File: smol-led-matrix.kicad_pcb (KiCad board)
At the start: 4 copper layers, 61.8 x 88.2 mm, 381 parts, among them J1 USB_C_Receptacle_USB2.0, J2 TagConnect_TC2030_SWD, Q1 FS8205, Q2 AO3401A, SW1 SW_Push, SW2 SW_Push, U1 STM32L433CBTx, U2 TP4054, U3 DW01+G, U4 XC6206P332MR

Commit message: Full panel
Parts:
- added C1: 100nF, Capacitor_SMD:C_0402_1005Metric, F.Cu at (94.8, 86.5)
- added C1: 100nF, Capacitor_SMD:C_0402_1005Metric, F.Cu at (94.8, 115.5)
- added C10: 10uF, Capacitor_SMD:C_0402_1005Metric, F.Cu at (99.9, 82.8)
- added C10: 10uF, Capacitor_SMD:C_0402_1005Metric, F.Cu at (99.9, 111.8)
- added C11: 100nF, Capacitor_SMD:C_0402_1005Metric, F.Cu at (88.2, 76.7)
- added C11: 100nF, Capacitor_SMD:C_0402_1005Metric, F.Cu at (88.2, 105.7)
- added C2: 100nF, Capacitor_SMD:C_0402_1005Metric, F.Cu at (88.0, 83.4)
- added C2: 100nF, Capacitor_SMD:C_0402_1005Metric, F.Cu at (88.0, 112.4)
- added C3: 1uF, Capacitor_SMD:C_0402_1005Metric, F.Cu at (100.5, 70.7)
- added C3: 1uF, Capacitor_SMD:C_0402_1005Metric, F.Cu at (100.5, 99.7)
- added C4: 100nF, Capacitor_SMD:C_0402_1005Metric, F.Cu at (107.0, 70.3)
- added C4: 100nF, Capacitor_SMD:C_0402_1005Metric, F.Cu at (107.0, 99.3)
- added C5: 100nF, Capacitor_SMD:C_0402_1005Metric, F.Cu at (93.0, 86.5)
- added C5: 100nF, Capacitor_SMD:C_0402_1005Metric, F.Cu at (93.0, 115.5)
- added C6: 1uF, Capacitor_SMD:C_0402_1005Metric, F.Cu at (101.9, 78.9)
- added C6: 1uF, Capacitor_SMD:C_0402_1005Metric, F.Cu at (101.9, 107.9)
- added C7: 1uF, Capacitor_SMD:C_0402_1005Metric, F.Cu at (103.6, 78.9)
- added C7: 1uF, Capacitor_SMD:C_0402_1005Metric, F.Cu at (103.6, 107.9)
- added C8: 100nF, Capacitor_SMD:C_0402_1005Metric, F.Cu at (89.2, 77.0)
- added C8: 100nF, Capacitor_SMD:C_0402_1005Metric, F.Cu at (89.2, 106.0)
- added C9: 100nF, Capacitor_SMD:C_0402_1005Metric, F.Cu at (97.5, 77.0)
- added C9: 100nF, Capacitor_SMD:C_0402_1005Metric, F.Cu at (97.5, 106.0)
- added D1: LED, LED_SMD:LED_0402_1005Metric, F.Cu at (63.2, 67.7)
- added D1: LED, LED_SMD:LED_0402_1005Metric, F.Cu at (63.2, 96.7)
- added D10: LED, LED_SMD:LED_0402_1005Metric, F.Cu at (63.2, 79.4)
- added D10: LED, LED_SMD:LED_0402_1005Metric, F.Cu at (63.2, 108.4)
- added D100: LED, LED_SMD:LED_0402_1005Metric, F.Cu at (71.0, 79.4)
- added D100: LED, LED_SMD:LED_0402_1005Metric, F.Cu at (71.0, 108.4)
- added D101: LED, LED_SMD:LED_0402_1005Metric, F.Cu at (71.0, 80.7)
- added D101: LED, LED_SMD:LED_0402_1005Metric, F.Cu at (71.0, 109.7)
- added D102: LED, LED_SMD:LED_0402_1005Metric, F.Cu at (71.0, 82.0)
- added D102: LED, LED_SMD:LED_0402_1005Metric, F.Cu at (71.0, 111.0)
- added D103: LED, LED_SMD:LED_0402_1005Metric, F.Cu at (71.0, 83.3)
- added D103: LED, LED_SMD:LED_0402_1005Metric, F.Cu at (71.0, 112.3)
- added D104: LED, LED_SMD:LED_0402_1005Metric, F.Cu at (71.0, 84.6)
- added D104: LED, LED_SMD:LED_0402_1005Metric, F.Cu at (71.0, 113.6)
- added D105: LED, LED_SMD:LED_0402_1005Metric, F.Cu at (71.0, 85.9)
- added D105: LED, LED_SMD:LED_0402_1005Metric, F.Cu at (71.0, 114.9)
- added D106: LED, LED_SMD:LED_0402_1005Metric, F.Cu at (72.3, 67.7)
- added D106: LED, LED_SMD:LED_0402_1005Metric, F.Cu at (72.3, 96.7)
- added D107: LED, LED_SMD:LED_0402_1005Metric, F.Cu at (72.3, 69.0)
- added D107: LED, LED_SMD:LED_0402_1005Metric, F.Cu at (72.3, 98.0)
- added D108: LED, LED_SMD:LED_0402_1005Metric, F.Cu at (72.3, 70.3)
- added D108: LED, LED_SMD:LED_0402_1005Metric, F.Cu at (72.3, 99.3)
- added D109: LED, LED_SMD:LED_0402_1005Metric, F.Cu at (72.3, 71.6)
- added D109: LED, LED_SMD:LED_0402_1005Metric, F.Cu at (72.3, 100.6)
- added D11: LED, LED_SMD:LED_0402_1005Metric, F.Cu at (63.2, 80.7)
- added D11: LED, LED_SMD:LED_0402_1005Metric, F.Cu at (63.2, 109.7)
- added D110: LED, LED_SMD:LED_0402_1005Metric, F.Cu at (72.3, 72.9)
- added D110: LED, LED_SMD:LED_0402_1005Metric, F.Cu at (72.3, 101.9)
- added D111: LED, LED_SMD:LED_0402_1005Metric, F.Cu at (72.3, 74.2)
- added D111: LED, LED_SMD:LED_0402_1005Metric, F.Cu at (72.3, 103.2)
- added D112: LED, LED_SMD:LED_0402_1005Metric, F.Cu at (72.3, 75.5)
- added D112: LED, LED_SMD:LED_0402_1005Metric, F.Cu at (72.3, 104.5)
- added D113: LED, LED_SMD:LED_0402_1005Metric, F.Cu at (72.3, 76.8)
- added D113: LED, LED_SMD:LED_0402_1005Metric, F.Cu at (72.3, 105.8)
- added D114: LED, LED_SMD:LED_0402_1005Metric, F.Cu at (72.3, 78.1)
- added D114: LED, LED_SMD:LED_0402_1005Metric, F.Cu at (72.3, 107.1)
- added D115: LED, LED_SMD:LED_0402_1005Metric, F.Cu at (72.3, 79.4)
- added D115: LED, LED_SMD:LED_0402_1005Metric, F.Cu at (72.3, 108.4)
- added D116: LED, LED_SMD:LED_0402_1005Metric, F.Cu at (72.3, 80.7)
- added D116: LED, LED_SMD:LED_0402_1005Metric, F.Cu at (72.3, 109.7)
- added D117: LED, LED_SMD:LED_0402_1005Metric, F.Cu at (72.3, 82.0)
- added D117: LED, LED_SMD:LED_0402_1005Metric, F.Cu at (72.3, 111.0)
- added D118: LED, LED_SMD:LED_0402_1005Metric, F.Cu at (72.3, 83.3)
- added D118: LED, LED_SMD:LED_0402_1005Metric, F.Cu at (72.3, 112.3)
- added D119: LED, LED_SMD:LED_0402_1005Metric, F.Cu at (72.3, 84.6)
- added D119: LED, LED_SMD:LED_0402_1005Metric, F.Cu at (72.3, 113.6)
- added D12: LED, LED_SMD:LED_0402_1005Metric, F.Cu at (63.2, 82.0)
- added D12: LED, LED_SMD:LED_0402_1005Metric, F.Cu at (63.2, 111.0)
- added D120: LED, LED_SMD:LED_0402_1005Metric, F.Cu at (72.3, 85.9)
- added D120: LED, LED_SMD:LED_0402_1005Metric, F.Cu at (72.3, 114.9)
- added D121: LED, LED_SMD:LED_0402_1005Metric, F.Cu at (73.6, 67.7)
- added D121: LED, LED_SMD:LED_0402_1005Metric, F.Cu at (73.6, 96.7)
- added D122: LED, LED_SMD:LED_0402_1005Metric, F.Cu at (73.6, 69.0)
- added D122: LED, LED_SMD:LED_0402_1005Metric, F.Cu at (73.6, 98.0)
- added D123: LED, LED_SMD:LED_0402_1005Metric, F.Cu at (73.6, 70.3)
- added D123: LED, LED_SMD:LED_0402_1005Metric, F.Cu at (73.6, 99.3)
- added D124: LED, LED_SMD:LED_0402_1005Metric, F.Cu at (73.6, 71.6)
- added D124: LED, LED_SMD:LED_0402_1005Metric, F.Cu at (73.6, 100.6)
- added D125: LED, LED_SMD:LED_0402_1005Metric, F.Cu at (73.6, 72.9)
- added D125: LED, LED_SMD:LED_0402_1005Metric, F.Cu at (73.6, 101.9)
- added D126: LED, LED_SMD:LED_0402_1005Metric, F.Cu at (73.6, 74.2)
- added D126: LED, LED_SMD:LED_0402_1005Metric, F.Cu at (73.6, 103.2)
- added D127: LED, LED_SMD:LED_0402_1005Metric, F.Cu at (73.6, 75.5)
- added D127: LED, LED_SMD:LED_0402_1005Metric, F.Cu at (73.6, 104.5)
- added D128: LED, LED_SMD:LED_0402_1005Metric, F.Cu at (73.6, 76.8)
- added D128: LED, LED_SMD:LED_0402_1005Metric, F.Cu at (73.6, 105.8)
- added D129: LED, LED_SMD:LED_0402_1005Metric, F.Cu at (73.6, 78.1)
- added D129: LED, LED_SMD:LED_0402_1005Metric, F.Cu at (73.6, 107.1)
- added D13: LED, LED_SMD:LED_0402_1005Metric, F.Cu at (63.2, 83.3)
- added D13: LED, LED_SMD:LED_0402_1005Metric, F.Cu at (63.2, 112.3)
- added D130: LED, LED_SMD:LED_0402_1005Metric, F.Cu at (73.6, 79.4)
- added D130: LED, LED_SMD:LED_0402_1005Metric, F.Cu at (73.6, 108.4)
- added D131: LED, LED_SMD:LED_0402_1005Metric, F.Cu at (73.6, 80.7)
- added D131: LED, LED_SMD:LED_0402_1005Metric, F.Cu at (73.6, 109.7)
- added D132: LED, LED_SMD:LED_0402_1005Metric, F.Cu at (73.6, 82.0)
- added D132: LED, LED_SMD:LED_0402_1005Metric, F.Cu at (73.6, 111.0)
- added D133: LED, LED_SMD:LED_0402_1005Metric, F.Cu at (73.6, 83.3)
- added D133: LED, LED_SMD:LED_0402_1005Metric, F.Cu at (73.6, 112.3)
- added D134: LED, LED_SMD:LED_0402_1005Metric, F.Cu at (73.6, 84.6)
- added D134: LED, LED_SMD:LED_0402_1005Metric, F.Cu at (73.6, 113.6)
- added D135: LED, LED_SMD:LED_0402_1005Metric, F.Cu at (73.6, 85.9)
- added D135: LED, LED_SMD:LED_0402_1005Metric, F.Cu at (73.6, 114.9)
- added D136: LED, LED_SMD:LED_0402_1005Metric, F.Cu at (74.9, 67.7)
- added D136: LED, LED_SMD:LED_0402_1005Metric, F.Cu at (74.9, 96.7)
- added D137: LED, LED_SMD:LED_0402_1005Metric, F.Cu at (74.9, 69.0)
- added D137: LED, LED_SMD:LED_0402_1005Metric, F.Cu at (74.9, 98.0)
- added D138: LED, LED_SMD:LED_0402_1005Metric, F.Cu at (74.9, 70.3)
- added D138: LED, LED_SMD:LED_0402_1005Metric, F.Cu at (74.9, 99.3)
- added D139: LED, LED_SMD:LED_0402_1005Metric, F.Cu at (74.9, 71.6)
- added D139: LED, LED_SMD:LED_0402_1005Metric, F.Cu at (74.9, 100.6)
- added D14: LED, LED_SMD:LED_0402_1005Metric, F.Cu at (63.2, 84.6)
- added D14: LED, LED_SMD:LED_0402_1005Metric, F.Cu at (63.2, 113.6)
- added D140: LED, LED_SMD:LED_0402_1005Metric, F.Cu at (74.9, 72.9)
- added D140: LED, LED_SMD:LED_0402_1005Metric, F.Cu at (74.9, 101.9)
- added D141: LED, LED_SMD:LED_0402_1005Metric, F.Cu at (74.9, 74.2)
- added D141: LED, LED_SMD:LED_0402_1005Metric, F.Cu at (74.9, 103.2)
- added D142: LED, LED_SMD:LED_0402_1005Metric, F.Cu at (74.9, 75.5)
- added D142: LED, LED_SMD:LED_0402_1005Metric, F.Cu at (74.9, 104.5)
- added D143: LED, LED_SMD:LED_0402_1005Metric, F.Cu at (74.9, 76.8)
- added D143: LED, LED_SMD:LED_0402_1005Metric, F.Cu at (74.9, 105.8)
- added D144: LED, LED_SMD:LED_0402_1005Metric, F.Cu at (74.9, 78.1)
- added D144: LED, LED_SMD:LED_0402_1005Metric, F.Cu at (74.9, 107.1)
- added D145: LED, LED_SMD:LED_0402_1005Metric, F.Cu at (74.9, 79.4)
- added D145: LED, LED_SMD:LED_0402_1005Metric, F.Cu at (74.9, 108.4)
- added D146: LED, LED_SMD:LED_0402_1005Metric, F.Cu at (74.9, 80.7)
- added D146: LED, LED_SMD:LED_0402_1005Metric, F.Cu at (74.9, 109.7)
- added D147: LED, LED_SMD:LED_0402_1005Metric, F.Cu at (74.9, 82.0)
- added D147: LED, LED_SMD:LED_0402_1005Metric, F.Cu at (74.9, 111.0)
- added D148: LED, LED_SMD:LED_0402_1005Metric, F.Cu at (74.9, 83.3)
- added D148: LED, LED_SMD:LED_0402_1005Metric, F.Cu at (74.9, 112.3)
- added D149: LED, LED_SMD:LED_0402_1005Metric, F.Cu at (74.9, 84.6)
- added D149: LED, LED_SMD:LED_0402_1005Metric, F.Cu at (74.9, 113.6)
- added D15: LED, LED_SMD:LED_0402_1005Metric, F.Cu at (63.2, 85.9)
- added D15: LED, LED_SMD:LED_0402_1005Metric, F.Cu at (63.2, 114.9)
- added D150: LED, LED_SMD:LED_0402_1005Metric, F.Cu at (74.9, 85.9)
- added D150: LED, LED_SMD:LED_0402_1005Metric, F.Cu at (74.9, 114.9)
- added D151: LED, LED_SMD:LED_0402_1005Metric, F.Cu at (76.2, 67.7)
- added D151: LED, LED_SMD:LED_0402_1005Metric, F.Cu at (76.2, 96.7)
- added D152: LED, LED_SMD:LED_0402_1005Metric, F.Cu at (76.2, 69.0)
- added D152: LED, LED_SMD:LED_0402_1005Metric, F.Cu at (76.2, 98.0)
- added D153: LED, LED_SMD:LED_0402_1005Metric, F.Cu at (76.2, 70.3)
- added D153: LED, LED_SMD:LED_0402_1005Metric, F.Cu at (76.2, 99.3)
- added D154: LED, LED_SMD:LED_0402_1005Metric, F.Cu at (76.2, 71.6)
- added D154: LED, LED_SMD:LED_0402_1005Metric, F.Cu at (76.2, 100.6)
- added D155: LED, LED_SMD:LED_0402_1005Metric, F.Cu at (76.2, 72.9)
- added D155: LED, LED_SMD:LED_0402_1005Metric, F.Cu at (76.2, 101.9)
- added D156: LED, LED_SMD:LED_0402_1005Metric, F.Cu at (76.2, 74.2)
- added D156: LED, LED_SMD:LED_0402_1005Metric, F.Cu at (76.2, 103.2)
- added D157: LED, LED_SMD:LED_0402_1005Metric, F.Cu at (76.2, 75.5)
- added D157: LED, LED_SMD:LED_0402_1005Metric, F.Cu at (76.2, 104.5)
- added D158: LED, LED_SMD:LED_0402_1005Metric, F.Cu at (76.2, 76.8)
- added D158: LED, LED_SMD:LED_0402_1005Metric, F.Cu at (76.2, 105.8)
- added D159: LED, LED_SMD:LED_0402_1005Metric, F.Cu at (76.2, 78.1)
- added D159: LED, LED_SMD:LED_0402_1005Metric, F.Cu at (76.2, 107.1)
- added D16: LED, LED_SMD:LED_0402_1005Metric, F.Cu at (64.5, 67.7)
- added D16: LED, LED_SMD:LED_0402_1005Metric, F.Cu at (64.5, 96.7)
- added D160: LED, LED_SMD:LED_0402_1005Metric, F.Cu at (76.2, 79.4)
- added D160: LED, LED_SMD:LED_0402_1005Metric, F.Cu at (76.2, 108.4)
- added D161: LED, LED_SMD:LED_0402_1005Metric, F.Cu at (76.2, 80.7)
- added D161: LED, LED_SMD:LED_0402_1005Metric, F.Cu at (76.2, 109.7)
- added D162: LED, LED_SMD:LED_0402_1005Metric, F.Cu at (76.2, 82.0)
- added D162: LED, LED_SMD:LED_0402_1005Metric, F.Cu at (76.2, 111.0)
- added D163: LED, LED_SMD:LED_0402_1005Metric, F.Cu at (76.2, 83.3)
- added D163: LED, LED_SMD:LED_0402_1005Metric, F.Cu at (76.2, 112.3)
- added D164: LED, LED_SMD:LED_0402_1005Metric, F.Cu at (76.2, 84.6)
- added D164: LED, LED_SMD:LED_0402_1005Metric, F.Cu at (76.2, 113.6)
- added D165: LED, LED_SMD:LED_0402_1005Metric, F.Cu at (76.2, 85.9)
- added D165: LED, LED_SMD:LED_0402_1005Metric, F.Cu at (76.2, 114.9)
- added D166: LED, LED_SMD:LED_0402_1005Metric, F.Cu at (77.5, 67.7)
- added D166: LED, LED_SMD:LED_0402_1005Metric, F.Cu at (77.5, 96.7)
- added D167: LED, LED_SMD:LED_0402_1005Metric, F.Cu at (77.5, 69.0)
- added D167: LED, LED_SMD:LED_0402_1005Metric, F.Cu at (77.5, 98.0)
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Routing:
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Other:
- outline, holes or cut-outs redrawn
- board text added: "SMØL MATRIX RevB Designed by Tobias Schramm 2020"
- board text removed: "SMØL MATRIX RevA Designed by Tobias Schramm 2020"

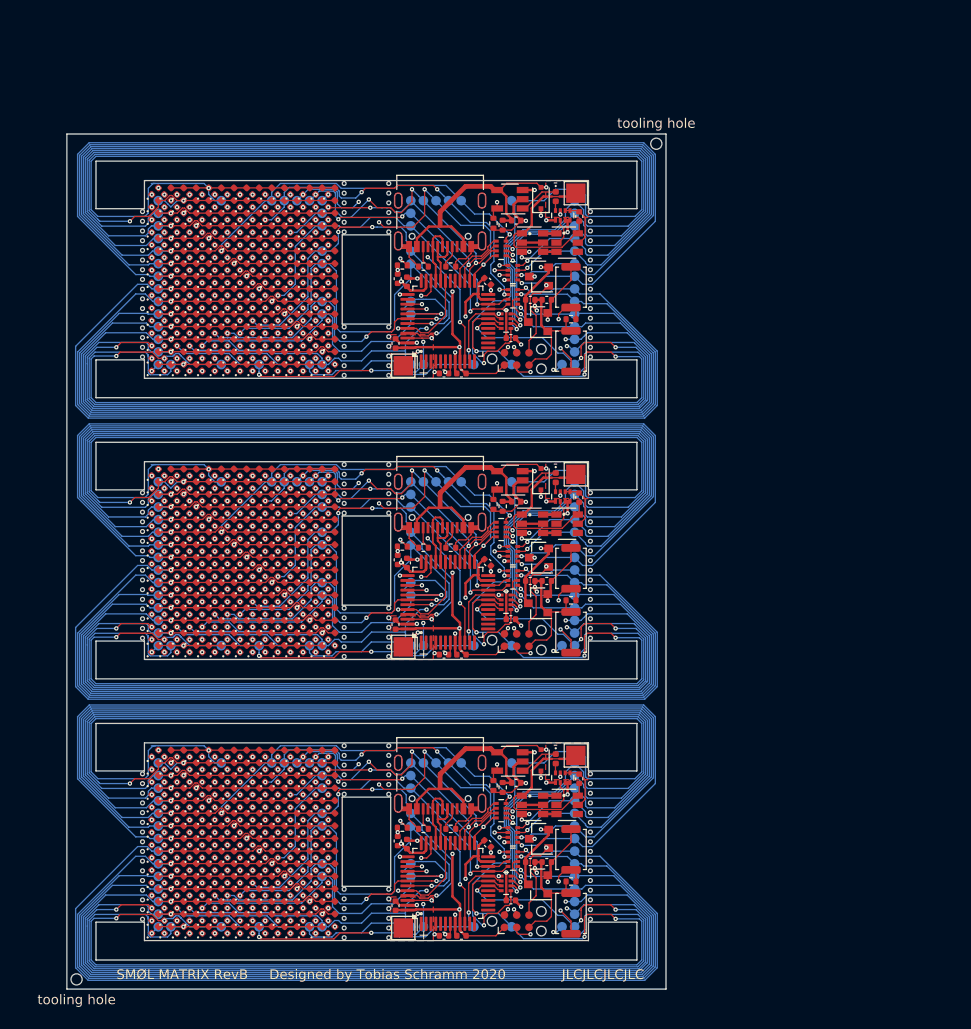
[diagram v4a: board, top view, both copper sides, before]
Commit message: Remove stubs and improve clearance around routed holes
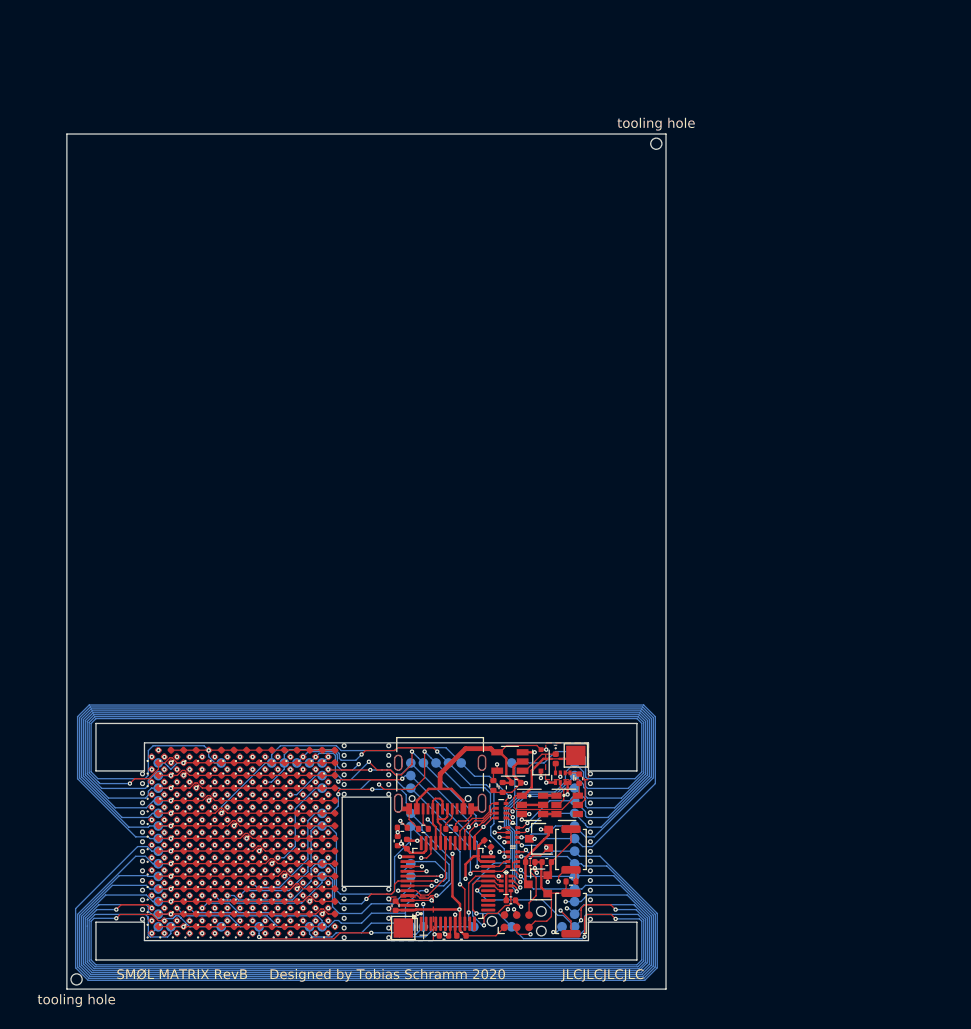
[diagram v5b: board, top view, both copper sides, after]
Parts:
- removed the C1 at (94.8, 86.5)
- removed the C1 at (94.8, 115.5)
- removed the C10 at (99.9, 82.8)
- removed the C10 at (99.9, 111.8)
- removed the C11 at (88.2, 76.7)
- removed the C11 at (88.2, 105.7)
- removed the C2 at (88.0, 83.4)
- removed the C2 at (88.0, 112.4)
- removed the C3 at (100.5, 70.7)
- removed the C3 at (100.5, 99.7)
- removed the C4 at (107.0, 70.3)
- removed the C4 at (107.0, 99.3)
- removed the C5 at (93.0, 86.5)
- removed the C5 at (93.0, 115.5)
- removed the C6 at (101.9, 78.9)
- removed the C6 at (101.9, 107.9)
- removed the C7 at (103.6, 78.9)
- removed the C7 at (103.6, 107.9)
- removed the C8 at (89.2, 77.0)
- removed the C8 at (89.2, 106.0)
- removed the C9 at (97.5, 77.0)
- removed the C9 at (97.5, 106.0)
- removed the D1 at (63.2, 67.7)
- removed the D1 at (63.2, 96.7)
- removed the D10 at (63.2, 79.4)
- removed the D10 at (63.2, 108.4)
- removed the D100 at (71.0, 79.4)
- removed the D100 at (71.0, 108.4)
- removed the D101 at (71.0, 80.7)
- removed the D101 at (71.0, 109.7)
- removed the D102 at (71.0, 82.0)
- removed the D102 at (71.0, 111.0)
- removed the D103 at (71.0, 83.3)
- removed the D103 at (71.0, 112.3)
- removed the D104 at (71.0, 84.6)
- removed the D104 at (71.0, 113.6)
- removed the D105 at (71.0, 85.9)
- removed the D105 at (71.0, 114.9)
- removed the D106 at (72.3, 67.7)
- removed the D106 at (72.3, 96.7)
- removed the D107 at (72.3, 69.0)
- removed the D107 at (72.3, 98.0)
- removed the D108 at (72.3, 70.3)
- removed the D108 at (72.3, 99.3)
- removed the D109 at (72.3, 71.6)
- removed the D109 at (72.3, 100.6)
- removed the D11 at (63.2, 80.7)
- removed the D11 at (63.2, 109.7)
- removed the D110 at (72.3, 72.9)
- removed the D110 at (72.3, 101.9)
- removed the D111 at (72.3, 74.2)
- removed the D111 at (72.3, 103.2)
- removed the D112 at (72.3, 75.5)
- removed the D112 at (72.3, 104.5)
- removed the D113 at (72.3, 76.8)
- removed the D113 at (72.3, 105.8)
- removed the D114 at (72.3, 78.1)
- removed the D114 at (72.3, 107.1)
- removed the D115 at (72.3, 79.4)
- removed the D115 at (72.3, 108.4)
- removed the D116 at (72.3, 80.7)
- removed the D116 at (72.3, 109.7)
- removed the D117 at (72.3, 82.0)
- removed the D117 at (72.3, 111.0)
- removed the D118 at (72.3, 83.3)
- removed the D118 at (72.3, 112.3)
- removed the D119 at (72.3, 84.6)
- removed the D119 at (72.3, 113.6)
- removed the D12 at (63.2, 82.0)
- removed the D12 at (63.2, 111.0)
- removed the D120 at (72.3, 85.9)
- removed the D120 at (72.3, 114.9)
- removed the D121 at (73.6, 67.7)
- removed the D121 at (73.6, 96.7)
- removed the D122 at (73.6, 69.0)
- removed the D122 at (73.6, 98.0)
- removed the D123 at (73.6, 70.3)
- removed the D123 at (73.6, 99.3)
- removed the D124 at (73.6, 71.6)
- removed the D124 at (73.6, 100.6)
- removed the D125 at (73.6, 72.9)
- removed the D125 at (73.6, 101.9)
- removed the D126 at (73.6, 74.2)
- removed the D126 at (73.6, 103.2)
- removed the D127 at (73.6, 75.5)
- removed the D127 at (73.6, 104.5)
- removed the D128 at (73.6, 76.8)
- removed the D128 at (73.6, 105.8)
- removed the D129 at (73.6, 78.1)
- removed the D129 at (73.6, 107.1)
- removed the D13 at (63.2, 83.3)
- removed the D13 at (63.2, 112.3)
- removed the D130 at (73.6, 79.4)
- removed the D130 at (73.6, 108.4)
- removed the D131 at (73.6, 80.7)
- removed the D131 at (73.6, 109.7)
- removed the D132 at (73.6, 82.0)
- removed the D132 at (73.6, 111.0)
- removed the D133 at (73.6, 83.3)
- removed the D133 at (73.6, 112.3)
- removed the D134 at (73.6, 84.6)
- removed the D134 at (73.6, 113.6)
- removed the D135 at (73.6, 85.9)
- removed the D135 at (73.6, 114.9)
- removed the D136 at (74.9, 67.7)
- removed the D136 at (74.9, 96.7)
- removed the D137 at (74.9, 69.0)
- removed the D137 at (74.9, 98.0)
- removed the D138 at (74.9, 70.3)
- removed the D138 at (74.9, 99.3)
- removed the D139 at (74.9, 71.6)
- removed the D139 at (74.9, 100.6)
- removed the D14 at (63.2, 84.6)
- removed the D14 at (63.2, 113.6)
- removed the D140 at (74.9, 72.9)
- removed the D140 at (74.9, 101.9)
- removed the D141 at (74.9, 74.2)
- removed the D141 at (74.9, 103.2)
- removed the D142 at (74.9, 75.5)
- removed the D142 at (74.9, 104.5)
- removed the D143 at (74.9, 76.8)
- removed the D143 at (74.9, 105.8)
- removed the D144 at (74.9, 78.1)
- removed the D144 at (74.9, 107.1)
- removed the D145 at (74.9, 79.4)
- removed the D145 at (74.9, 108.4)
- removed the D146 at (74.9, 80.7)
- removed the D146 at (74.9, 109.7)
- removed the D147 at (74.9, 82.0)
- removed the D147 at (74.9, 111.0)
- removed the D148 at (74.9, 83.3)
- removed the D148 at (74.9, 112.3)
- removed the D149 at (74.9, 84.6)
- removed the D149 at (74.9, 113.6)
- removed the D15 at (63.2, 85.9)
- removed the D15 at (63.2, 114.9)
- removed the D150 at (74.9, 85.9)
- removed the D150 at (74.9, 114.9)
- removed the D151 at (76.2, 67.7)
- removed the D151 at (76.2, 96.7)
- removed the D152 at (76.2, 69.0)
- removed the D152 at (76.2, 98.0)
- removed the D153 at (76.2, 70.3)
- removed the D153 at (76.2, 99.3)
- removed the D154 at (76.2, 71.6)
- removed the D154 at (76.2, 100.6)
- removed the D155 at (76.2, 72.9)
- removed the D155 at (76.2, 101.9)
- removed the D156 at (76.2, 74.2)
- removed the D156 at (76.2, 103.2)
- removed the D157 at (76.2, 75.5)
- removed the D157 at (76.2, 104.5)
- removed the D158 at (76.2, 76.8)
- removed the D158 at (76.2, 105.8)
- removed the D159 at (76.2, 78.1)
- removed the D159 at (76.2, 107.1)
- removed the D16 at (64.5, 67.7)
- removed the D16 at (64.5, 96.7)
- removed the D160 at (76.2, 79.4)
- removed the D160 at (76.2, 108.4)
- removed the D161 at (76.2, 80.7)
- removed the D161 at (76.2, 109.7)
- removed the D162 at (76.2, 82.0)
- removed the D162 at (76.2, 111.0)
- removed the D163 at (76.2, 83.3)
- removed the D163 at (76.2, 112.3)
- removed the D164 at (76.2, 84.6)
- removed the D164 at (76.2, 113.6)
- removed the D165 at (76.2, 85.9)
- removed the D165 at (76.2, 114.9)
- removed the D166 at (77.5, 67.7)
- removed the D166 at (77.5, 96.7)
- removed the D167 at (77.5, 69.0)
- removed the D167 at (77.5, 98.0)
- removed the D168 at (77.5, 70.3)
- removed the D168 at (77.5, 99.3)
- removed the D169 at (77.5, 71.6)
- removed the D169 at (77.5, 100.6)
- removed the D17 at (64.5, 69.0)
- removed the D17 at (64.5, 98.0)
- removed the D170 at (77.5, 72.9)
- removed the D170 at (77.5, 101.9)
- removed the D171 at (77.5, 74.2)
- removed the D171 at (77.5, 103.2)
- removed the D172 at (77.5, 75.5)
- removed the D172 at (77.5, 104.5)
- removed the D173 at (77.5, 76.8)
- removed the D173 at (77.5, 105.8)
- removed the D174 at (77.5, 78.1)
- removed the D174 at (77.5, 107.1)
- removed the D175 at (77.5, 79.4)
- removed the D175 at (77.5, 108.4)
- removed the D176 at (77.5, 80.7)
- removed the D176 at (77.5, 109.7)
- removed the D177 at (77.5, 82.0)
- removed the D177 at (77.5, 111.0)
- removed the D178 at (77.5, 83.3)
- removed the D178 at (77.5, 112.3)
- removed the D179 at (77.5, 84.6)
- removed the D179 at (77.5, 113.6)
- removed the D18 at (64.5, 70.3)
- removed the D18 at (64.5, 99.3)
- removed the D180 at (77.5, 85.9)
- removed the D180 at (77.5, 114.9)
- removed the D181 at (78.8, 67.7)
- removed the D181 at (78.8, 96.7)
- removed the D182 at (78.8, 69.0)
- removed the D182 at (78.8, 98.0)
- removed the D183 at (78.8, 70.3)
- removed the D183 at (78.8, 99.3)
- removed the D184 at (78.8, 71.6)
- removed the D184 at (78.8, 100.6)
- removed the D185 at (78.8, 72.9)
- removed the D185 at (78.8, 101.9)
- removed the D186 at (78.8, 74.2)
- removed the D186 at (78.8, 103.2)
- removed the D187 at (78.8, 75.5)
- removed the D187 at (78.8, 104.5)
- removed the D188 at (78.8, 76.8)
- removed the D188 at (78.8, 105.8)
- removed the D189 at (78.8, 78.1)
- removed the D189 at (78.8, 107.1)
- removed the D19 at (64.5, 71.6)
- removed the D19 at (64.5, 100.6)
- removed the D190 at (78.8, 79.4)
- removed the D190 at (78.8, 108.4)
- removed the D191 at (78.8, 80.7)
- removed the D191 at (78.8, 109.7)
- removed the D192 at (78.8, 82.0)
- removed the D192 at (78.8, 111.0)
- removed the D193 at (78.8, 83.3)
- removed the D193 at (78.8, 112.3)
- removed the D194 at (78.8, 84.6)
- removed the D194 at (78.8, 113.6)
- removed the D195 at (78.8, 85.9)
- removed the D195 at (78.8, 114.9)
- removed the D196 at (80.1, 67.7)
- removed the D196 at (80.1, 96.7)
- removed the D197 at (80.1, 69.0)
- removed the D197 at (80.1, 98.0)
- removed the D198 at (80.1, 70.3)
- removed the D198 at (80.1, 99.3)
- removed the D199 at (80.1, 71.6)
- removed the D199 at (80.1, 100.6)
- removed the D2 at (63.2, 69.0)
- removed the D2 at (63.2, 98.0)
- removed the D20 at (64.5, 72.9)
- removed the D20 at (64.5, 101.9)
- removed the D200 at (80.1, 72.9)
- removed the D200 at (80.1, 101.9)
- removed the D201 at (80.1, 74.2)
- removed the D201 at (80.1, 103.2)
- removed the D202 at (80.1, 75.5)
- removed the D202 at (80.1, 104.5)
- removed the D203 at (80.1, 76.8)
- removed the D203 at (80.1, 105.8)
- removed the D204 at (80.1, 78.1)
- removed the D204 at (80.1, 107.1)
- removed the D205 at (80.1, 79.4)
- removed the D205 at (80.1, 108.4)
- removed the D206 at (80.1, 80.7)
- removed the D206 at (80.1, 109.7)
- removed the D207 at (80.1, 82.0)
- removed the D207 at (80.1, 111.0)
- removed the D208 at (80.1, 83.3)
- removed the D208 at (80.1, 112.3)
- removed the D209 at (80.1, 84.6)
- removed the D209 at (80.1, 113.6)
- removed the D21 at (64.5, 74.2)
- removed the D21 at (64.5, 103.2)
- removed the D210 at (80.1, 85.9)
- removed the D210 at (80.1, 114.9)
- removed the D211 at (81.4, 67.7)
- removed the D211 at (81.4, 96.7)
- removed the D212 at (81.4, 69.0)
- removed the D212 at (81.4, 98.0)
- removed the D213 at (81.4, 70.3)
- removed the D213 at (81.4, 99.3)
- removed the D214 at (81.4, 71.6)
- removed the D214 at (81.4, 100.6)
- removed the D215 at (81.4, 72.9)
- removed the D215 at (81.4, 101.9)
- removed the D216 at (81.4, 74.2)
- removed the D216 at (81.4, 103.2)
- removed the D217 at (81.4, 75.5)
- removed the D217 at (81.4, 104.5)
- removed the D218 at (81.4, 76.8)
- removed the D218 at (81.4, 105.8)
- removed the D219 at (81.4, 78.1)
- removed the D219 at (81.4, 107.1)
- removed the D22 at (64.5, 75.5)
- removed the D22 at (64.5, 104.5)
- removed the D220 at (81.4, 79.4)
- removed the D220 at (81.4, 108.4)
- removed the D221 at (81.4, 80.7)
- removed the D221 at (81.4, 109.7)
- removed the D222 at (81.4, 82.0)
- removed the D222 at (81.4, 111.0)
- removed the D223 at (81.4, 83.3)
- removed the D223 at (81.4, 112.3)
- removed the D224 at (81.4, 84.6)
- removed the D224 at (81.4, 113.6)
- removed the D225 at (81.4, 85.9)
- removed the D225 at (81.4, 114.9)
- removed the D226 at (104.5, 68.2)
- removed the D226 at (104.5, 97.2)
- removed the D227 at (103.0, 68.4)
- removed the D227 at (103.0, 97.4)
- removed the D23 at (64.5, 76.8)
- removed the D23 at (64.5, 105.8)
- removed the D24 at (64.5, 78.1)
- removed the D24 at (64.5, 107.1)
- removed the D25 at (64.5, 79.4)
- removed the D25 at (64.5, 108.4)
- removed the D26 at (64.5, 80.7)
- removed the D26 at (64.5, 109.7)
- removed the D27 at (64.5, 82.0)
- removed the D27 at (64.5, 111.0)
- removed the D28 at (64.5, 83.3)
- removed the D28 at (64.5, 112.3)
- removed the D29 at (64.5, 84.6)
- removed the D29 at (64.5, 113.6)
- removed the D3 at (63.2, 70.3)
- removed the D3 at (63.2, 99.3)
- removed the D30 at (64.5, 85.9)
- removed the D30 at (64.5, 114.9)
- removed the D31 at (65.8, 67.7)
- removed the D31 at (65.8, 96.7)
- removed the D32 at (65.8, 69.0)
- removed the D32 at (65.8, 98.0)
- removed the D33 at (65.8, 70.3)
- removed the D33 at (65.8, 99.3)
- removed the D34 at (65.8, 71.6)
- removed the D34 at (65.8, 100.6)
- removed the D35 at (65.8, 72.9)
- removed the D35 at (65.8, 101.9)
- removed the D36 at (65.8, 74.2)
- removed the D36 at (65.8, 103.2)
- removed the D37 at (65.8, 75.5)
- removed the D37 at (65.8, 104.5)
- removed the D38 at (65.8, 76.8)
- removed the D38 at (65.8, 105.8)
- removed the D39 at (65.8, 78.1)
- removed the D39 at (65.8, 107.1)
- removed the D4 at (63.2, 71.6)
- removed the D4 at (63.2, 100.6)
- removed the D40 at (65.8, 79.4)
- removed the D40 at (65.8, 108.4)
- removed the D41 at (65.8, 80.7)
- removed the D41 at (65.8, 109.7)
- removed the D42 at (65.8, 82.0)
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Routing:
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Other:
- outline, holes or cut-outs redrawn

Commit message: Repanelize
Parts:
- added C1: 100nF, Capacitor_SMD:C_0402_1005Metric, F.Cu at (94.8, 86.5)
- added C1: 100nF, Capacitor_SMD:C_0402_1005Metric, F.Cu at (94.8, 115.5)
- added C10: 10uF, Capacitor_SMD:C_0402_1005Metric, F.Cu at (99.9, 82.8)
- added C10: 10uF, Capacitor_SMD:C_0402_1005Metric, F.Cu at (99.9, 111.8)
- added C11: 100nF, Capacitor_SMD:C_0402_1005Metric, F.Cu at (88.2, 76.7)
- added C11: 100nF, Capacitor_SMD:C_0402_1005Metric, F.Cu at (88.2, 105.7)
- added C2: 100nF, Capacitor_SMD:C_0402_1005Metric, F.Cu at (88.0, 83.4)
- added C2: 100nF, Capacitor_SMD:C_0402_1005Metric, F.Cu at (88.0, 112.4)
- added C3: 1uF, Capacitor_SMD:C_0402_1005Metric, F.Cu at (100.5, 70.7)
- added C3: 1uF, Capacitor_SMD:C_0402_1005Metric, F.Cu at (100.5, 99.7)
- added C4: 100nF, Capacitor_SMD:C_0402_1005Metric, F.Cu at (107.0, 70.3)
- added C4: 100nF, Capacitor_SMD:C_0402_1005Metric, F.Cu at (107.0, 99.3)
- added C5: 100nF, Capacitor_SMD:C_0402_1005Metric, F.Cu at (93.0, 86.5)
- added C5: 100nF, Capacitor_SMD:C_0402_1005Metric, F.Cu at (93.0, 115.5)
- added C6: 1uF, Capacitor_SMD:C_0402_1005Metric, F.Cu at (101.9, 78.9)
- added C6: 1uF, Capacitor_SMD:C_0402_1005Metric, F.Cu at (101.9, 107.9)
- added C7: 1uF, Capacitor_SMD:C_0402_1005Metric, F.Cu at (103.6, 78.9)
- added C7: 1uF, Capacitor_SMD:C_0402_1005Metric, F.Cu at (103.6, 107.9)
- added C8: 100nF, Capacitor_SMD:C_0402_1005Metric, F.Cu at (89.2, 77.0)
- added C8: 100nF, Capacitor_SMD:C_0402_1005Metric, F.Cu at (89.2, 106.0)
- added C9: 100nF, Capacitor_SMD:C_0402_1005Metric, F.Cu at (97.5, 77.0)
- added C9: 100nF, Capacitor_SMD:C_0402_1005Metric, F.Cu at (97.5, 106.0)
- added D1: LED, LED_SMD:LED_0402_1005Metric, F.Cu at (63.2, 67.7)
- added D1: LED, LED_SMD:LED_0402_1005Metric, F.Cu at (63.2, 96.7)
- added D10: LED, LED_SMD:LED_0402_1005Metric, F.Cu at (63.2, 79.4)
- added D10: LED, LED_SMD:LED_0402_1005Metric, F.Cu at (63.2, 108.4)
- added D100: LED, LED_SMD:LED_0402_1005Metric, F.Cu at (71.0, 79.4)
- added D100: LED, LED_SMD:LED_0402_1005Metric, F.Cu at (71.0, 108.4)
- added D101: LED, LED_SMD:LED_0402_1005Metric, F.Cu at (71.0, 80.7)
- added D101: LED, LED_SMD:LED_0402_1005Metric, F.Cu at (71.0, 109.7)
- added D102: LED, LED_SMD:LED_0402_1005Metric, F.Cu at (71.0, 82.0)
- added D102: LED, LED_SMD:LED_0402_1005Metric, F.Cu at (71.0, 111.0)
- added D103: LED, LED_SMD:LED_0402_1005Metric, F.Cu at (71.0, 83.3)
- added D103: LED, LED_SMD:LED_0402_1005Metric, F.Cu at (71.0, 112.3)
- added D104: LED, LED_SMD:LED_0402_1005Metric, F.Cu at (71.0, 84.6)
- added D104: LED, LED_SMD:LED_0402_1005Metric, F.Cu at (71.0, 113.6)
- added D105: LED, LED_SMD:LED_0402_1005Metric, F.Cu at (71.0, 85.9)
- added D105: LED, LED_SMD:LED_0402_1005Metric, F.Cu at (71.0, 114.9)
- added D106: LED, LED_SMD:LED_0402_1005Metric, F.Cu at (72.3, 67.7)
- added D106: LED, LED_SMD:LED_0402_1005Metric, F.Cu at (72.3, 96.7)
- added D107: LED, LED_SMD:LED_0402_1005Metric, F.Cu at (72.3, 69.0)
- added D107: LED, LED_SMD:LED_0402_1005Metric, F.Cu at (72.3, 98.0)
- added D108: LED, LED_SMD:LED_0402_1005Metric, F.Cu at (72.3, 70.3)
- added D108: LED, LED_SMD:LED_0402_1005Metric, F.Cu at (72.3, 99.3)
- added D109: LED, LED_SMD:LED_0402_1005Metric, F.Cu at (72.3, 71.6)
- added D109: LED, LED_SMD:LED_0402_1005Metric, F.Cu at (72.3, 100.6)
- added D11: LED, LED_SMD:LED_0402_1005Metric, F.Cu at (63.2, 80.7)
- added D11: LED, LED_SMD:LED_0402_1005Metric, F.Cu at (63.2, 109.7)
- added D110: LED, LED_SMD:LED_0402_1005Metric, F.Cu at (72.3, 72.9)
- added D110: LED, LED_SMD:LED_0402_1005Metric, F.Cu at (72.3, 101.9)
- added D111: LED, LED_SMD:LED_0402_1005Metric, F.Cu at (72.3, 74.2)
- added D111: LED, LED_SMD:LED_0402_1005Metric, F.Cu at (72.3, 103.2)
- added D112: LED, LED_SMD:LED_0402_1005Metric, F.Cu at (72.3, 75.5)
- added D112: LED, LED_SMD:LED_0402_1005Metric, F.Cu at (72.3, 104.5)
- added D113: LED, LED_SMD:LED_0402_1005Metric, F.Cu at (72.3, 76.8)
- added D113: LED, LED_SMD:LED_0402_1005Metric, F.Cu at (72.3, 105.8)
- added D114: LED, LED_SMD:LED_0402_1005Metric, F.Cu at (72.3, 78.1)
- added D114: LED, LED_SMD:LED_0402_1005Metric, F.Cu at (72.3, 107.1)
- added D115: LED, LED_SMD:LED_0402_1005Metric, F.Cu at (72.3, 79.4)
- added D115: LED, LED_SMD:LED_0402_1005Metric, F.Cu at (72.3, 108.4)
- added D116: LED, LED_SMD:LED_0402_1005Metric, F.Cu at (72.3, 80.7)
- added D116: LED, LED_SMD:LED_0402_1005Metric, F.Cu at (72.3, 109.7)
- added D117: LED, LED_SMD:LED_0402_1005Metric, F.Cu at (72.3, 82.0)
- added D117: LED, LED_SMD:LED_0402_1005Metric, F.Cu at (72.3, 111.0)
- added D118: LED, LED_SMD:LED_0402_1005Metric, F.Cu at (72.3, 83.3)
- added D118: LED, LED_SMD:LED_0402_1005Metric, F.Cu at (72.3, 112.3)
- added D119: LED, LED_SMD:LED_0402_1005Metric, F.Cu at (72.3, 84.6)
- added D119: LED, LED_SMD:LED_0402_1005Metric, F.Cu at (72.3, 113.6)
- added D12: LED, LED_SMD:LED_0402_1005Metric, F.Cu at (63.2, 82.0)
- added D12: LED, LED_SMD:LED_0402_1005Metric, F.Cu at (63.2, 111.0)
- added D120: LED, LED_SMD:LED_0402_1005Metric, F.Cu at (72.3, 85.9)
- added D120: LED, LED_SMD:LED_0402_1005Metric, F.Cu at (72.3, 114.9)
- added D121: LED, LED_SMD:LED_0402_1005Metric, F.Cu at (73.6, 67.7)
- added D121: LED, LED_SMD:LED_0402_1005Metric, F.Cu at (73.6, 96.7)
- added D122: LED, LED_SMD:LED_0402_1005Metric, F.Cu at (73.6, 69.0)
- added D122: LED, LED_SMD:LED_0402_1005Metric, F.Cu at (73.6, 98.0)
- added D123: LED, LED_SMD:LED_0402_1005Metric, F.Cu at (73.6, 70.3)
- added D123: LED, LED_SMD:LED_0402_1005Metric, F.Cu at (73.6, 99.3)
- added D124: LED, LED_SMD:LED_0402_1005Metric, F.Cu at (73.6, 71.6)
- added D124: LED, LED_SMD:LED_0402_1005Metric, F.Cu at (73.6, 100.6)
- added D125: LED, LED_SMD:LED_0402_1005Metric, F.Cu at (73.6, 72.9)
- added D125: LED, LED_SMD:LED_0402_1005Metric, F.Cu at (73.6, 101.9)
- added D126: LED, LED_SMD:LED_0402_1005Metric, F.Cu at (73.6, 74.2)
- added D126: LED, LED_SMD:LED_0402_1005Metric, F.Cu at (73.6, 103.2)
- added D127: LED, LED_SMD:LED_0402_1005Metric, F.Cu at (73.6, 75.5)
- added D127: LED, LED_SMD:LED_0402_1005Metric, F.Cu at (73.6, 104.5)
- added D128: LED, LED_SMD:LED_0402_1005Metric, F.Cu at (73.6, 76.8)
- added D128: LED, LED_SMD:LED_0402_1005Metric, F.Cu at (73.6, 105.8)
- added D129: LED, LED_SMD:LED_0402_1005Metric, F.Cu at (73.6, 78.1)
- added D129: LED, LED_SMD:LED_0402_1005Metric, F.Cu at (73.6, 107.1)
- added D13: LED, LED_SMD:LED_0402_1005Metric, F.Cu at (63.2, 83.3)
- added D13: LED, LED_SMD:LED_0402_1005Metric, F.Cu at (63.2, 112.3)
- added D130: LED, LED_SMD:LED_0402_1005Metric, F.Cu at (73.6, 79.4)
- added D130: LED, LED_SMD:LED_0402_1005Metric, F.Cu at (73.6, 108.4)
- added D131: LED, LED_SMD:LED_0402_1005Metric, F.Cu at (73.6, 80.7)
- added D131: LED, LED_SMD:LED_0402_1005Metric, F.Cu at (73.6, 109.7)
- added D132: LED, LED_SMD:LED_0402_1005Metric, F.Cu at (73.6, 82.0)
- added D132: LED, LED_SMD:LED_0402_1005Metric, F.Cu at (73.6, 111.0)
- added D133: LED, LED_SMD:LED_0402_1005Metric, F.Cu at (73.6, 83.3)
- added D133: LED, LED_SMD:LED_0402_1005Metric, F.Cu at (73.6, 112.3)
- added D134: LED, LED_SMD:LED_0402_1005Metric, F.Cu at (73.6, 84.6)
- added D134: LED, LED_SMD:LED_0402_1005Metric, F.Cu at (73.6, 113.6)
- added D135: LED, LED_SMD:LED_0402_1005Metric, F.Cu at (73.6, 85.9)
- added D135: LED, LED_SMD:LED_0402_1005Metric, F.Cu at (73.6, 114.9)
- added D136: LED, LED_SMD:LED_0402_1005Metric, F.Cu at (74.9, 67.7)
- added D136: LED, LED_SMD:LED_0402_1005Metric, F.Cu at (74.9, 96.7)
- added D137: LED, LED_SMD:LED_0402_1005Metric, F.Cu at (74.9, 69.0)
- added D137: LED, LED_SMD:LED_0402_1005Metric, F.Cu at (74.9, 98.0)
- added D138: LED, LED_SMD:LED_0402_1005Metric, F.Cu at (74.9, 70.3)
- added D138: LED, LED_SMD:LED_0402_1005Metric, F.Cu at (74.9, 99.3)
- added D139: LED, LED_SMD:LED_0402_1005Metric, F.Cu at (74.9, 71.6)
- added D139: LED, LED_SMD:LED_0402_1005Metric, F.Cu at (74.9, 100.6)
- added D14: LED, LED_SMD:LED_0402_1005Metric, F.Cu at (63.2, 84.6)
- added D14: LED, LED_SMD:LED_0402_1005Metric, F.Cu at (63.2, 113.6)
- added D140: LED, LED_SMD:LED_0402_1005Metric, F.Cu at (74.9, 72.9)
- added D140: LED, LED_SMD:LED_0402_1005Metric, F.Cu at (74.9, 101.9)
- added D141: LED, LED_SMD:LED_0402_1005Metric, F.Cu at (74.9, 74.2)
- added D141: LED, LED_SMD:LED_0402_1005Metric, F.Cu at (74.9, 103.2)
- added D142: LED, LED_SMD:LED_0402_1005Metric, F.Cu at (74.9, 75.5)
- added D142: LED, LED_SMD:LED_0402_1005Metric, F.Cu at (74.9, 104.5)
- added D143: LED, LED_SMD:LED_0402_1005Metric, F.Cu at (74.9, 76.8)
- added D143: LED, LED_SMD:LED_0402_1005Metric, F.Cu at (74.9, 105.8)
- added D144: LED, LED_SMD:LED_0402_1005Metric, F.Cu at (74.9, 78.1)
- added D144: LED, LED_SMD:LED_0402_1005Metric, F.Cu at (74.9, 107.1)
- added D145: LED, LED_SMD:LED_0402_1005Metric, F.Cu at (74.9, 79.4)
- added D145: LED, LED_SMD:LED_0402_1005Metric, F.Cu at (74.9, 108.4)
- added D146: LED, LED_SMD:LED_0402_1005Metric, F.Cu at (74.9, 80.7)
- added D146: LED, LED_SMD:LED_0402_1005Metric, F.Cu at (74.9, 109.7)
- added D147: LED, LED_SMD:LED_0402_1005Metric, F.Cu at (74.9, 82.0)
- added D147: LED, LED_SMD:LED_0402_1005Metric, F.Cu at (74.9, 111.0)
- added D148: LED, LED_SMD:LED_0402_1005Metric, F.Cu at (74.9, 83.3)
- added D148: LED, LED_SMD:LED_0402_1005Metric, F.Cu at (74.9, 112.3)
- added D149: LED, LED_SMD:LED_0402_1005Metric, F.Cu at (74.9, 84.6)
- added D149: LED, LED_SMD:LED_0402_1005Metric, F.Cu at (74.9, 113.6)
- added D15: LED, LED_SMD:LED_0402_1005Metric, F.Cu at (63.2, 85.9)
- added D15: LED, LED_SMD:LED_0402_1005Metric, F.Cu at (63.2, 114.9)
- added D150: LED, LED_SMD:LED_0402_1005Metric, F.Cu at (74.9, 85.9)
- added D150: LED, LED_SMD:LED_0402_1005Metric, F.Cu at (74.9, 114.9)
- added D151: LED, LED_SMD:LED_0402_1005Metric, F.Cu at (76.2, 67.7)
- added D151: LED, LED_SMD:LED_0402_1005Metric, F.Cu at (76.2, 96.7)
- added D152: LED, LED_SMD:LED_0402_1005Metric, F.Cu at (76.2, 69.0)
- added D152: LED, LED_SMD:LED_0402_1005Metric, F.Cu at (76.2, 98.0)
- added D153: LED, LED_SMD:LED_0402_1005Metric, F.Cu at (76.2, 70.3)
- added D153: LED, LED_SMD:LED_0402_1005Metric, F.Cu at (76.2, 99.3)
- added D154: LED, LED_SMD:LED_0402_1005Metric, F.Cu at (76.2, 71.6)
- added D154: LED, LED_SMD:LED_0402_1005Metric, F.Cu at (76.2, 100.6)
- added D155: LED, LED_SMD:LED_0402_1005Metric, F.Cu at (76.2, 72.9)
- added D155: LED, LED_SMD:LED_0402_1005Metric, F.Cu at (76.2, 101.9)
- added D156: LED, LED_SMD:LED_0402_1005Metric, F.Cu at (76.2, 74.2)
- added D156: LED, LED_SMD:LED_0402_1005Metric, F.Cu at (76.2, 103.2)
- added D157: LED, LED_SMD:LED_0402_1005Metric, F.Cu at (76.2, 75.5)
- added D157: LED, LED_SMD:LED_0402_1005Metric, F.Cu at (76.2, 104.5)
- added D158: LED, LED_SMD:LED_0402_1005Metric, F.Cu at (76.2, 76.8)
- added D158: LED, LED_SMD:LED_0402_1005Metric, F.Cu at (76.2, 105.8)
- added D159: LED, LED_SMD:LED_0402_1005Metric, F.Cu at (76.2, 78.1)
- added D159: LED, LED_SMD:LED_0402_1005Metric, F.Cu at (76.2, 107.1)
- added D16: LED, LED_SMD:LED_0402_1005Metric, F.Cu at (64.5, 67.7)
- added D16: LED, LED_SMD:LED_0402_1005Metric, F.Cu at (64.5, 96.7)
- added D160: LED, LED_SMD:LED_0402_1005Metric, F.Cu at (76.2, 79.4)
- added D160: LED, LED_SMD:LED_0402_1005Metric, F.Cu at (76.2, 108.4)
- added D161: LED, LED_SMD:LED_0402_1005Metric, F.Cu at (76.2, 80.7)
- added D161: LED, LED_SMD:LED_0402_1005Metric, F.Cu at (76.2, 109.7)
- added D162: LED, LED_SMD:LED_0402_1005Metric, F.Cu at (76.2, 82.0)
- added D162: LED, LED_SMD:LED_0402_1005Metric, F.Cu at (76.2, 111.0)
- added D163: LED, LED_SMD:LED_0402_1005Metric, F.Cu at (76.2, 83.3)
- added D163: LED, LED_SMD:LED_0402_1005Metric, F.Cu at (76.2, 112.3)
- added D164: LED, LED_SMD:LED_0402_1005Metric, F.Cu at (76.2, 84.6)
- added D164: LED, LED_SMD:LED_0402_1005Metric, F.Cu at (76.2, 113.6)
- added D165: LED, LED_SMD:LED_0402_1005Metric, F.Cu at (76.2, 85.9)
- added D165: LED, LED_SMD:LED_0402_1005Metric, F.Cu at (76.2, 114.9)
- added D166: LED, LED_SMD:LED_0402_1005Metric, F.Cu at (77.5, 67.7)
- added D166: LED, LED_SMD:LED_0402_1005Metric, F.Cu at (77.5, 96.7)
- added D167: LED, LED_SMD:LED_0402_1005Metric, F.Cu at (77.5, 69.0)
- added D167: LED, LED_SMD:LED_0402_1005Metric, F.Cu at (77.5, 98.0)
- added D168: LED, LED_SMD:LED_0402_1005Metric, F.Cu at (77.5, 70.3)
- added D168: LED, LED_SMD:LED_0402_1005Metric, F.Cu at (77.5, 99.3)
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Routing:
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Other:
- outline, holes or cut-outs redrawn
